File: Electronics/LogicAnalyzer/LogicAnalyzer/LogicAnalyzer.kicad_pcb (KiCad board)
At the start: 2 copper layers, 57 x 55.2 mm, 6 parts, among them J1 Conn_02x15_Odd_Even, U1 Pico

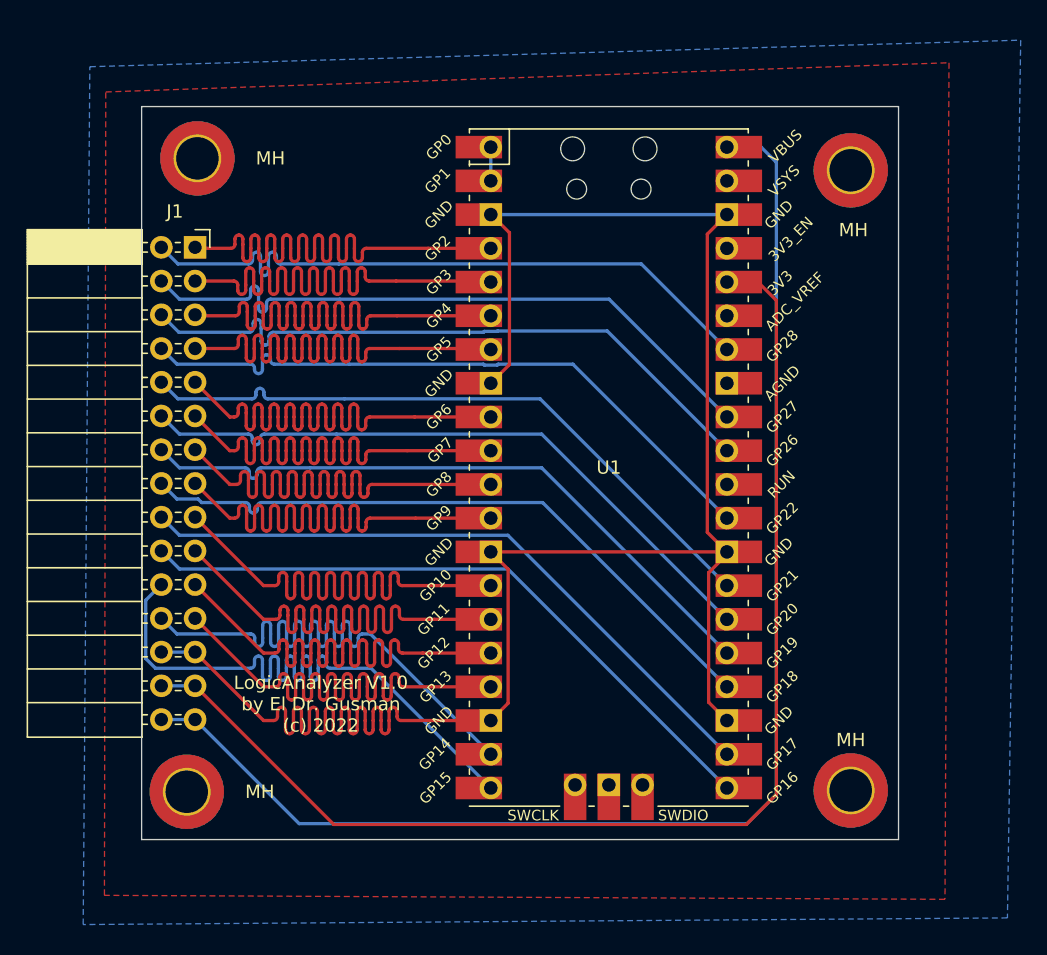
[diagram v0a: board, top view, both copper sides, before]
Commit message: New external trigger
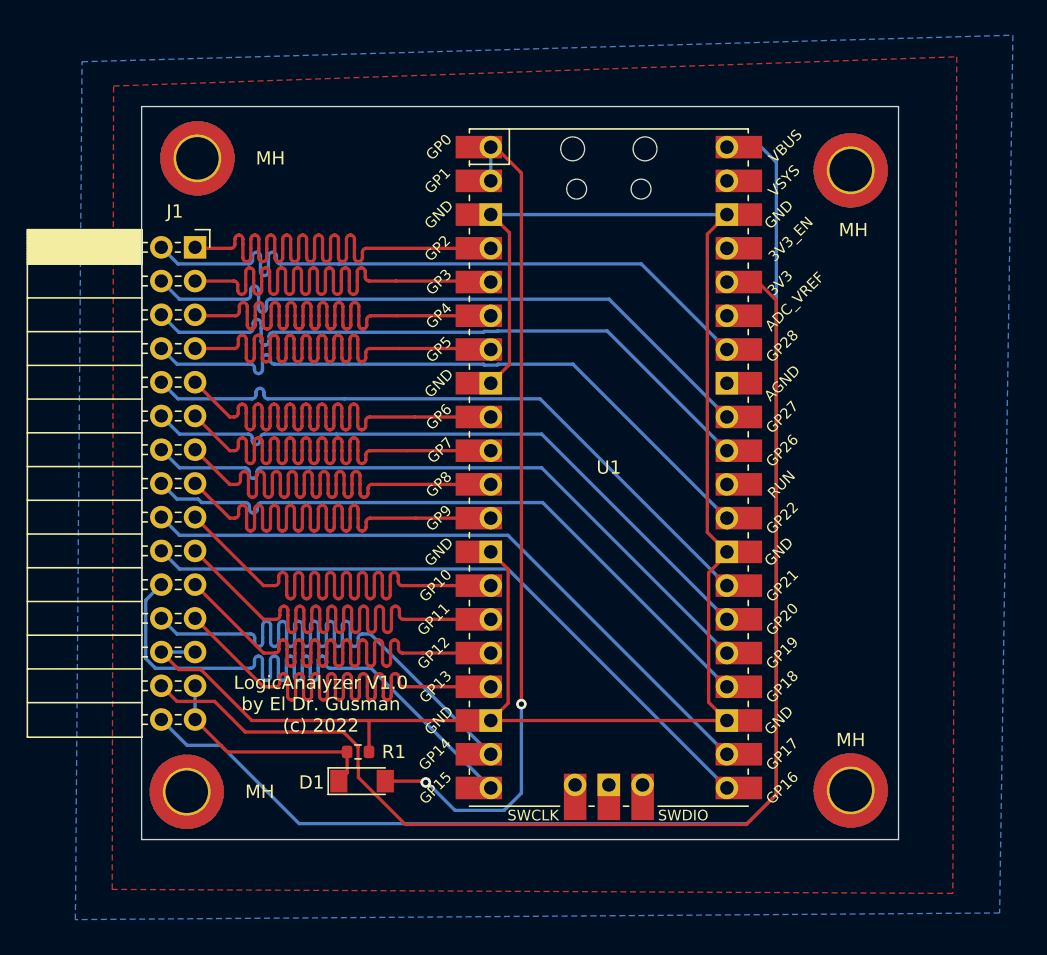
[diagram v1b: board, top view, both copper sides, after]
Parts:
- added D1: LL4148, Diode_SMD:D_MiniMELF, F.Cu at (89.6, 112.4)
- added R1: 100k, Resistor_SMD:R_0603_1608Metric, F.Cu at (89.3, 110.2)
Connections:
- J1 pad 27: /3V3 -> /EXT_T
- J1 pad 29: /5V -> /EXT_T
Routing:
- net Net-(U1-Pad1): track 2.54 -> 64.1 mm, vias 0 -> 2
- net /GND: track 155.8 -> 135.6 mm
- net /EXT_T: track 0.00 -> 17.5 mm
- net /3V3: track 93.1 -> 94.4 mm

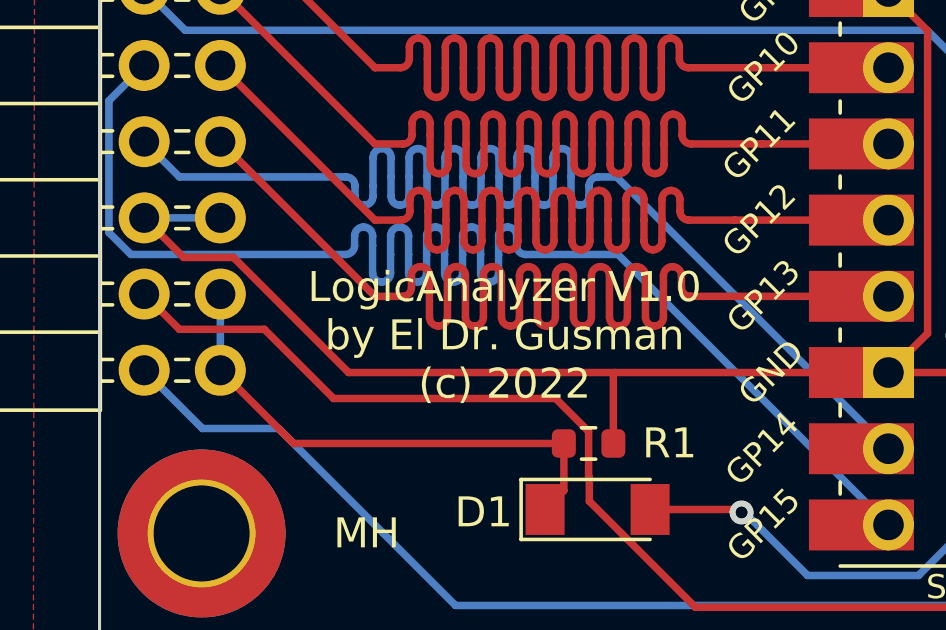
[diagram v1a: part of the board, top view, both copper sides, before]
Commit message: Updated pcb texts to new version
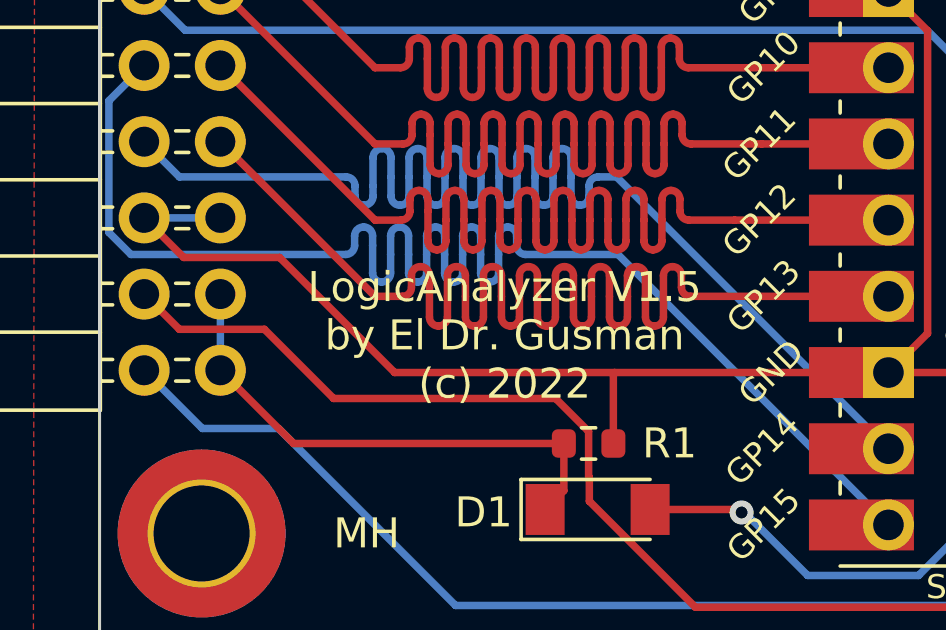
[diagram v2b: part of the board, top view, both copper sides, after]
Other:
- board text added: "LogicAnalyzer V1.5 by El Dr. Gusman (c) 2022"
- board text removed: "LogicAnalyzer V1.0 by El Dr. Gusman (c) 2022"
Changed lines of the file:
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@@
   )
   (gr_rect (start 130 61.6) (end 73 116.8) (layer "Edge.Cuts") (width 0.1) (fill none))
-  (gr_text "LogicAnalyzer V1.0\nby El Dr. Gusman\n(c) 2022" (at 86.5 106.6) (layer "F.SilkS")
+  (gr_text "LogicAnalyzer V1.5\nby El Dr. Gusman\n(c) 2022" (at 86.5 106.6) (layer "F.SilkS")
     (effects (font (size 1 1) (thickness 0.15)))
   )
@@
   (segment (start 99.295 69.735) (end 99.335 69.735) (width 0.25) (layer "F.Cu") (net 25))
   (segment (start 100.7 81.03) (end 99.295 82.435) (width 0.25) (layer "F.Cu") (net 25))
+  (segment (start 82.835 107.835) (end 79 104) (width 0.25) (layer "F.Cu") (net 25))
   (segment (start 90.125 107.875) (end 90.165 107.835) (width 0.25) (layer "F.Cu") (net 25))
   (segment (start 99.295 107.835) (end 90.165 107.835) (width 0.25) (layer "F.Cu") (net 25))
+  (segment (start 90.125 110.2) (end 90.125 107.875) (width 0.25) (layer "F.Cu") (net 25))
   (segment (start 75.805 104) (end 74.485 102.68) (width 0.25) (layer "F.Cu") (net 25))
-  (segment (start 90.125 110.2) (end 90.125 107.875) (width 0.25) (layer "F.Cu") (net 25))
   (segment (start 117.075 69.735) (end 115.6 71.21) (width 0.25) (layer "F.Cu") (net 25))
   (segment (start 115.7 96.700978) (end 115.7 106.46) (width 0.25) (layer "F.Cu") (net 25))
@@
   (segment (start 99.295 95.135) (end 100.6 96.44) (width 0.25) (layer "F.Cu") (net 25))
   (segment (start 100.6 96.44) (end 100.6 106.53) (width 0.25) (layer "F.Cu") (net 25))
-  (segment (start 90.165 107.835) (end 81.30101 107.835) (width 0.25) (layer "F.Cu") (net 25))
   (segment (start 115.6 71.21) (end 115.6 93.66) (width 0.25) (layer "F.Cu") (net 25))
   (segment (start 100.6 106.53) (end 99.295 107.835) (width 0.25) (layer "F.Cu") (net 25))
-  (segment (start 77.46601 104) (end 75.805 104) (width 0.25) (layer "F.Cu") (net 25))
   (segment (start 99.295 107.835) (end 117.075 107.835) (width 0.25) (layer "F.Cu") (net 25))
   (segment (start 117.075 95.325978) (end 115.7 96.700978) (width 0.25) (layer "F.Cu") (net 25))
@@
   (segment (start 115.7 106.46) (end 117.075 107.835) (width 0.25) (layer "F.Cu") (net 25))
   (segment (start 100.7 71.1) (end 100.7 81.03) (width 0.25) (layer "F.Cu") (net 25))
-  (segment (start 81.30101 107.835) (end 77.46601 104) (width 0.25) (layer "F.Cu") (net 25))
+  (segment (start 79 104) (end 75.805 104) (width 0.25) (layer "F.Cu") (net 25))
+  (segment (start 90.165 107.835) (end 82.835 107.835) (width 0.25) (layer "F.Cu") (net 25))
   (segment (start 77.025 102.68) (end 74.485 102.68) (width 0.25) (layer "B.Cu") (net 25))
   (segment (start 99.295 69.735) (end 117.075 69.735) (width 0.25) (layer "B.Cu") (net 25))

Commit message: Version 4.0
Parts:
- added J2: Conn_01x03, Connector_PinSocket_2.54mm:PinSocket_1x03_P2.54mm_Horizontal, F.Cu at (87.5, 65.7)
- added J3: Conn_01x03, Connector_PinHeader_2.54mm:PinHeader_1x03_P2.54mm_Horizontal, F.Cu at (87.5, 112.7)
- moved R1 5.12 mm to (85.0, 107.5)
- moved D1 4.80 mm to (85.7, 109.6)
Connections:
- net Net-(U1-Pad1) renamed /EXT_CHAIN
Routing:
- net /GND: track 135.6 -> 156.7 mm
- net /EXT_CHAIN: track 64.1 -> 83.2 mm, vias 2 -> 1
- net /EXT_T: track 17.5 -> 12.3 mm
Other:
- board text added: "LogicAnalyzer V4.0 by El Dr. Gusman (c) 2023"
- board text removed: "LogicAnalyzer V1.5 by El Dr. Gusman (c) 2022"
